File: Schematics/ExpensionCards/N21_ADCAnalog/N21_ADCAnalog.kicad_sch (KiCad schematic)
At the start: 67 parts

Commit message: Reworked N20/N21
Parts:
- JP2101: renamed from JP1; value Jumper_2_Small_Bridged -> A; footprint TestPoint:TestPoint_Bridge_Pitch2.54mm_Drill1.0mm -> TestPoint:TestPoint_Bridge_Pitch5.08mm_Drill0.7mm; symbol Jumper:Jumper_2_Small_Bridged -> Jumper:Jumper_2_Small_Open
- JP2102: renamed from JP2; value Jumper_2_Small_Bridged -> B; footprint TestPoint:TestPoint_Bridge_Pitch2.54mm_Drill1.0mm -> TestPoint:TestPoint_Bridge_Pitch5.08mm_Drill0.7mm; symbol Jumper:Jumper_2_Small_Bridged -> Jumper:Jumper_2_Small_Open
- JP2103: renamed from JP3; value Jumper_2_Small_Bridged -> C; footprint TestPoint:TestPoint_Bridge_Pitch2.54mm_Drill1.0mm -> TestPoint:TestPoint_Bridge_Pitch5.08mm_Drill0.7mm; symbol Jumper:Jumper_2_Small_Bridged -> Jumper:Jumper_2_Small_Open
- JP2104: renamed from JP4; value Jumper_2_Small_Bridged -> D; footprint TestPoint:TestPoint_Bridge_Pitch2.54mm_Drill1.0mm -> TestPoint:TestPoint_Bridge_Pitch5.08mm_Drill0.7mm; symbol Jumper:Jumper_2_Small_Bridged -> Jumper:Jumper_2_Small_Open
- R2104, R2115, R2118, R2121: footprint PM2528:Potentiometer horizontal ceramic -> PM2528:Trimmer vertical
- R2111: value 5k9 -> 5k90
- TP2101, TP2102, TP2103, TP2104, TP2105, TP2106, TP2107, TP2108, TP2109: footprint Connector_Pin:Pin_D1.0mm_L10.0mm -> Connector_Pin:Pin_D0.9mm_L10.0mm_W2.4mm_FlatFork
- renumbered K1 to X2101
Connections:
- net at A2102.6, C2103.1, R2109.1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: no longer A2102.1 (BAL), C2105.1
- new net: A2102.1 (BAL), C2105.1
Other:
- company: (none) -> D. Kupers
- moved on the sheet: A2101, A2102, A2103, A2104, A2105, A2106, C2103, C2104, C2105, C2106, C2112, C2113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

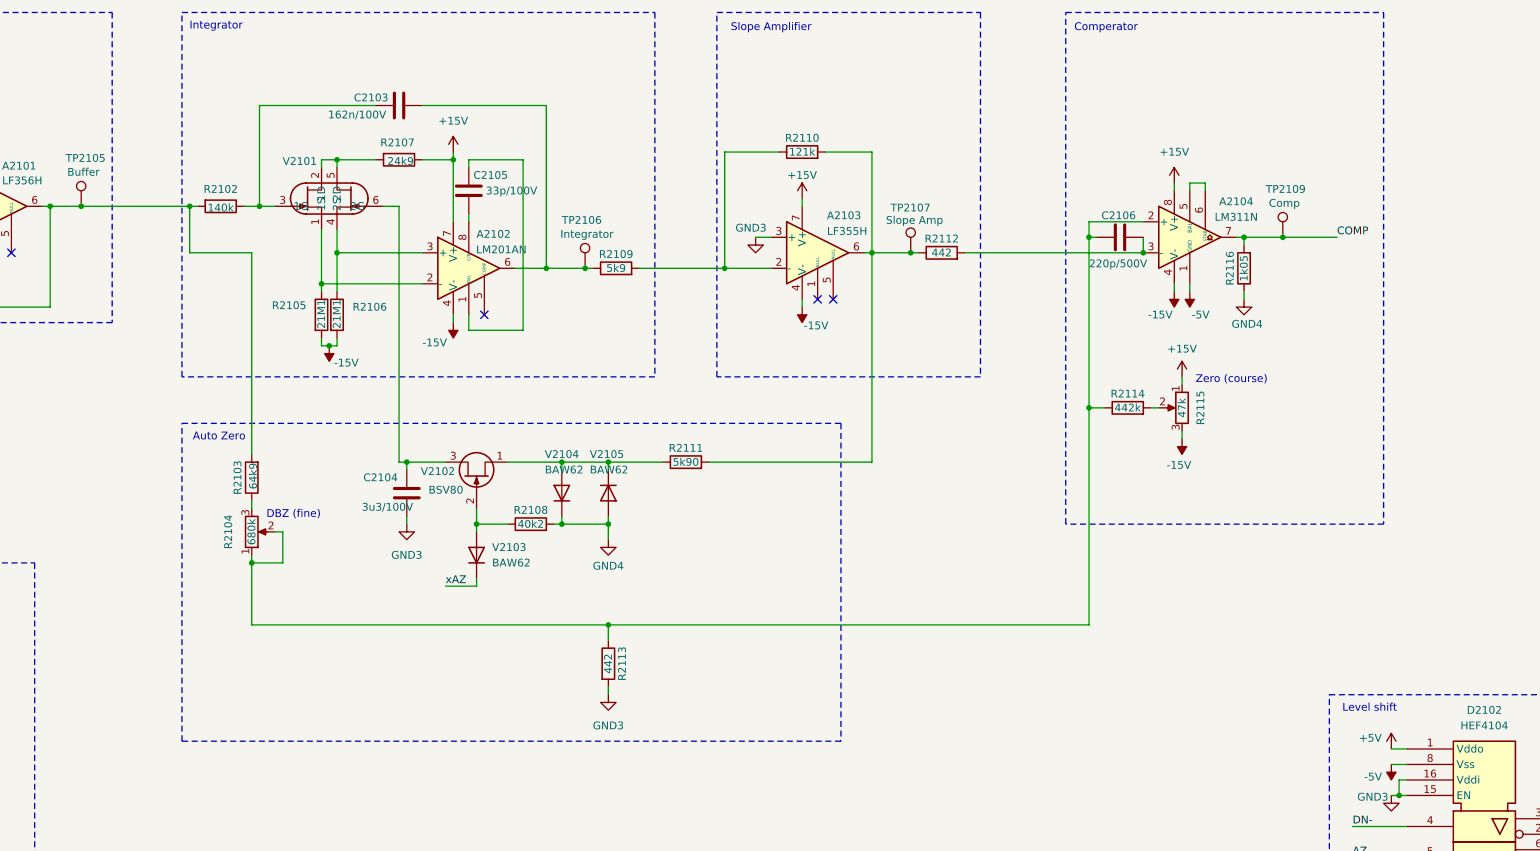
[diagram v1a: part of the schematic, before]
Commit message: Updated some component-values
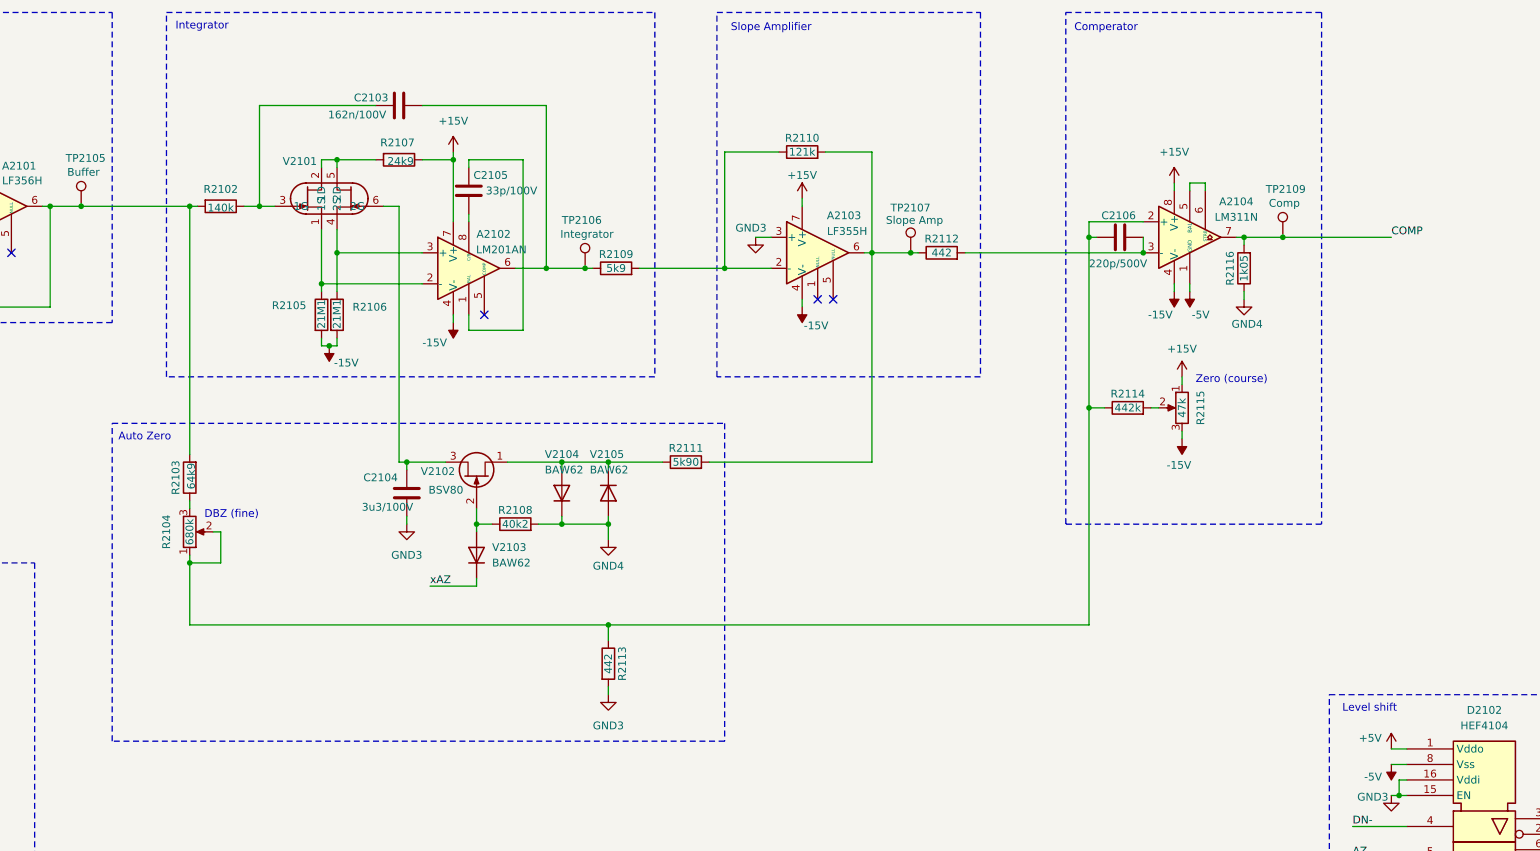
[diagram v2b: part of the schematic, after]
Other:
- moved on the sheet: R2103, R2104, R2108
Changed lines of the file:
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@@
 	)
 	(rectangle
-		(start 165.1 13.97)
+		(start 162.56 13.97)
 		(end 242.57 73.66)
 		(stroke
@@
 	)
 	(rectangle
-		(start 165.1 81.28)
-		(end 273.05 133.35)
+		(start 153.67 81.28)
+		(end 254 133.35)
 		(stroke
 			(width 0)
@@
 	(rectangle
 		(start 309.88 13.97)
-		(end 361.95 97.79)
+		(end 351.79 97.79)
 		(stroke
 			(width 0)
@@
 	(text "Integrator"
 		(exclude_from_sim no)
-		(at 170.688 16.256 0)
+		(at 168.402 16.256 0)
 		(effects
 			(font
@@
 	(text "DBZ (fine)"
 		(exclude_from_sim no)
-		(at 183.388 96.266 0)
+		(at 173.228 96.266 0)
 		(effects
 			(font
@@
 	(text "Auto Zero"
 		(exclude_from_sim no)
-		(at 171.196 83.566 0)
+		(at 159.004 83.566 0)
 		(effects
 			(font
@@
 	)
 	(junction
-		(at 176.53 104.14)
+		(at 166.37 104.14)
 		(diameter 0)
 		(color 0 0 0 0)
@@
 	(wire
 		(pts
-			(xy 176.53 114.3) (xy 234.95 114.3)
+			(xy 166.37 114.3) (xy 234.95 114.3)
 		)
 		(stroke
@@
 	(wire
 		(pts
-			(xy 226.06 97.79) (xy 227.33 97.79)
+			(xy 223.52 97.79) (xy 227.33 97.79)
 		)
 		(stroke
@@
 	(wire
 		(pts
-			(xy 181.61 99.06) (xy 181.61 104.14)
+			(xy 171.45 99.06) (xy 171.45 104.14)
 		)
 		(stroke
@@
 	(wire
 		(pts
-			(xy 176.53 86.36) (xy 176.53 53.34)
+			(xy 166.37 45.72) (xy 166.37 86.36)
 		)
 		(stroke
@@
 	(wire
 		(pts
-			(xy 208.28 107.95) (xy 213.36 107.95)
+			(xy 205.74 107.95) (xy 213.36 107.95)
 		)
 		(stroke
@@
 	(wire
 		(pts
-			(xy 166.37 53.34) (xy 166.37 45.72)
-		)
-		(stroke
-			(width 0)
-			(type default)
-		)
-	)
-	(wire
-		(pts
-			(xy 345.44 50.8) (xy 354.33 50.8)
-		)
-		(stroke
-			(width 0)
-			(type default)
-		)
-	)
-	(wire
-		(pts
 			(xy 105.41 151.13) (xy 105.41 167.64)
 		)
@@
 	(wire
 		(pts
-			(xy 176.53 104.14) (xy 176.53 114.3)
+			(xy 166.37 104.14) (xy 166.37 114.3)
 		)
 		(stroke
@@
 	(wire
 		(pts
-			(xy 176.53 102.87) (xy 176.53 104.14)
+			(xy 166.37 102.87) (xy 166.37 104.14)
 		)
 		(stroke
@@
 	(wire
 		(pts
-			(xy 176.53 93.98) (xy 176.53 95.25)
+			(xy 166.37 93.98) (xy 166.37 95.25)
 		)
 		(stroke
@@
 	(wire
 		(pts
-			(xy 218.44 97.79) (xy 213.36 97.79)
+			(xy 215.9 97.79) (xy 213.36 97.79)
 		)
 		(stroke
@@
 	(wire
 		(pts
-			(xy 180.34 99.06) (xy 181.61 99.06)
+			(xy 170.18 99.06) (xy 171.45 99.06)
 		)
 		(stroke
@@
 	(wire
 		(pts
+			(xy 345.44 50.8) (xy 363.22 50.8)
+		)
+		(stroke
+			(width 0)
+			(type default)
+		)
+	)
+	(wire
+		(pts
 			(xy 66.04 151.13) (xy 66.04 149.86)
 		)
@@
 	(wire
 		(pts
-			(xy 176.53 53.34) (xy 166.37 53.34)
-		)
-		(stroke
-			(width 0)
-			(type default)
-		)
-	)
-	(wire
-		(pts
 			(xy 80.01 135.89) (xy 82.55 135.89)
 		)
@@
 	(wire
 		(pts
-			(xy 181.61 104.14) (xy 176.53 104.14)
+			(xy 171.45 104.14) (xy 166.37 104.14)
 		)
 		(stroke
@@
 	)
 	(label "xAZ"
-		(at 208.28 107.95 0)
+		(at 205.74 107.95 0)
 		(effects
 			(font
@@
 	)
 	(label "COMP"
-		(at 354.33 50.8 0)
+		(at 363.22 50.8 0)
 		(effects
 			(font
@@
 	(symbol
 		(lib_id "Device:R")
-		(at 222.25 97.79 90)
+		(at 219.71 97.79 90)
 		(unit 1)
 		(exclude_from_sim no)
@@
 		(dnp no)
 		(property "Reference" "R2108"
-			(at 222.25 95.504 90)
+			(at 219.71 95.504 90)
 			(effects
 				(font
@@
 		)
 		(property "Value" "40k2"
-			(at 222.25 97.79 90)
+			(at 219.71 97.79 90)
 			(effects
 				(font
@@
 		)
 		(property "Footprint" "Resistor_THT:R_Axial_DIN0207_L6.3mm_D2.5mm_P10.16mm_Horizontal"
-			(at 222.25 99.568 90)
+			(at 219.71 99.568 90)
 			(effects
 				(font
@@
 		)
 		(property "Datasheet" "~"
-			(at 222.25 97.79 0)
+			(at 219.71 97.79 0)
 			(effects
 				(font
@@
 		)
 		(property "Description" "Resistor"
-			(at 222.25 97.79 0)
+			(at 219.71 97.79 0)
 			(effects
 				(font
@@
 	(symbol
 		(lib_id "Device:R_Potentiometer")
-		(at 176.53 99.06 0)
+		(at 166.37 99.06 0)
 		(mirror x)
 		(unit 1)
@@
 		(dnp no)
 		(property "Reference" "R2104"
-			(at 172.72 99.06 90)
+			(at 162.56 99.06 90)
 			(effects
 				(font
@@
 		)
 		(property "Value" "680k"
-			(at 176.53 99.06 90)
+			(at 166.37 99.06 90)
 			(effects
 				(font
@@
 		)
 		(property "Footprint" "PM2528:Trimmer vertical"
-			(at 176.53 99.06 0)
+			(at 166.37 99.06 0)
 			(effects
 				(font
@@
 		)
 		(property "Datasheet" "~"
-			(at 176.53 99.06 0)
+			(at 166.37 99.06 0)
 			(effects
 				(font
@@
 		)
 		(property "Description" "Potentiometer"
-			(at 176.53 99.06 0)
+			(at 166.37 99.06 0)
 			(effects
 				(font
@@
 	(symbol
 		(lib_id "Device:R")
-		(at 176.53 90.17 180)
+		(at 166.37 90.17 180)
 		(unit 1)
 		(exclude_from_sim no)
@@
 		(dnp no)
 		(property "Reference" "R2103"
-			(at 174.244 90.17 90)
+			(at 164.084 90.17 90)
 			(effects
 				(font
@@
 		)
 		(property "Value" "64k9"
-			(at 176.784 89.916 90)
+			(at 166.624 89.916 90)
 			(effects
 				(font
@@
 		)
 		(property "Footprint" "Resistor_THT:R_Axial_DIN0207_L6.3mm_D2.5mm_P10.16mm_Horizontal"
-			(at 178.308 90.17 90)
+			(at 168.148 90.17 90)
 			(effects
 				(font
@@
 		)
 		(property "Datasheet" "~"
-			(at 176.53 90.17 0)
+			(at 166.37 90.17 0)
 			(effects
 				(font
@@
 		)
 		(property "Description" "Resistor"
-			(at 176.53 90.17 0)
+			(at 166.37 90.17 0)
 			(effects
 				(font
